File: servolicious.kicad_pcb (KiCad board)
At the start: 2 copper layers, 57.5 x 27.5 mm, 14 parts, among them J1 Conn_01x03_Pin, J10 Barrel_Jack_MountingPin, J2 Conn_01x03_Pin, J3 Conn_01x03_Pin, J4 Conn_01x03_Pin, J5 Conn_01x03_Pin, J6 Conn_01x03_Pin, J7 Conn_01x03_Pin, J8 Conn_01x03_Pin, J9 Conn_01x03_Pin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

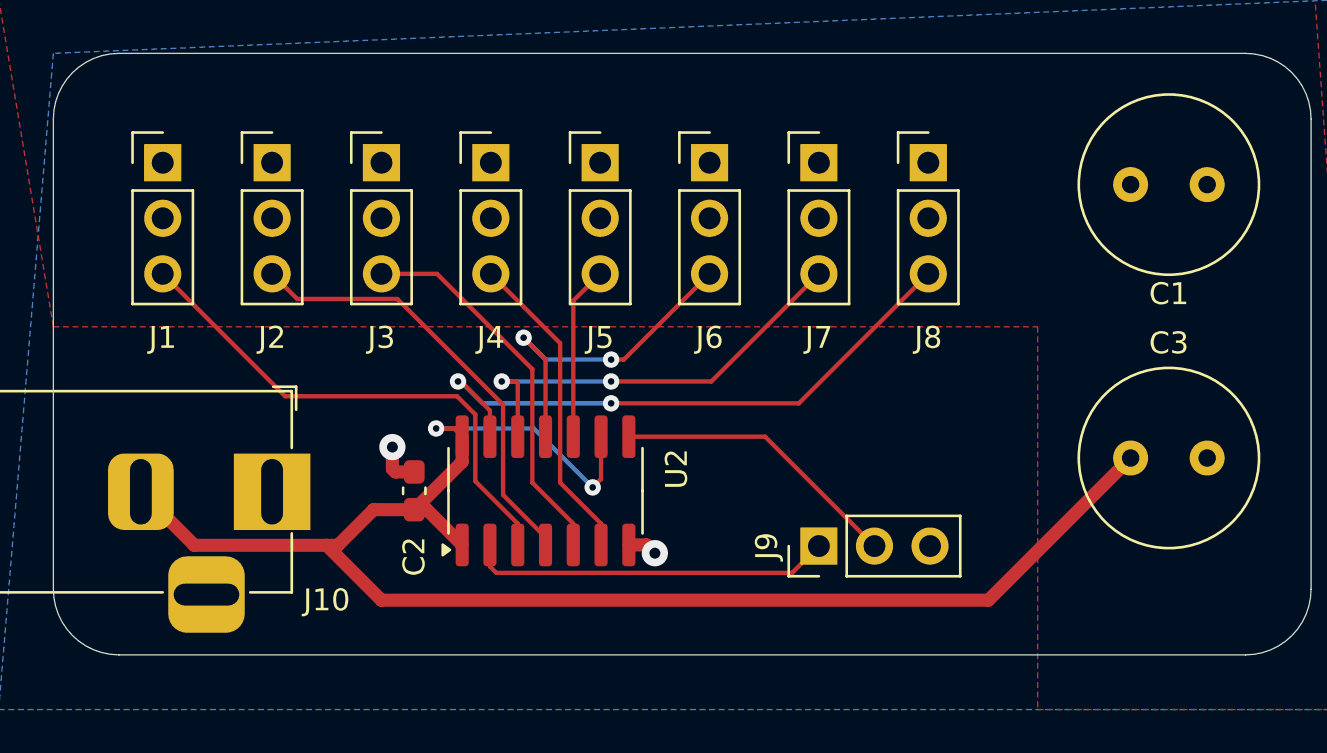
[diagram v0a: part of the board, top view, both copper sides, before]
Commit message: Switch to latched shift register
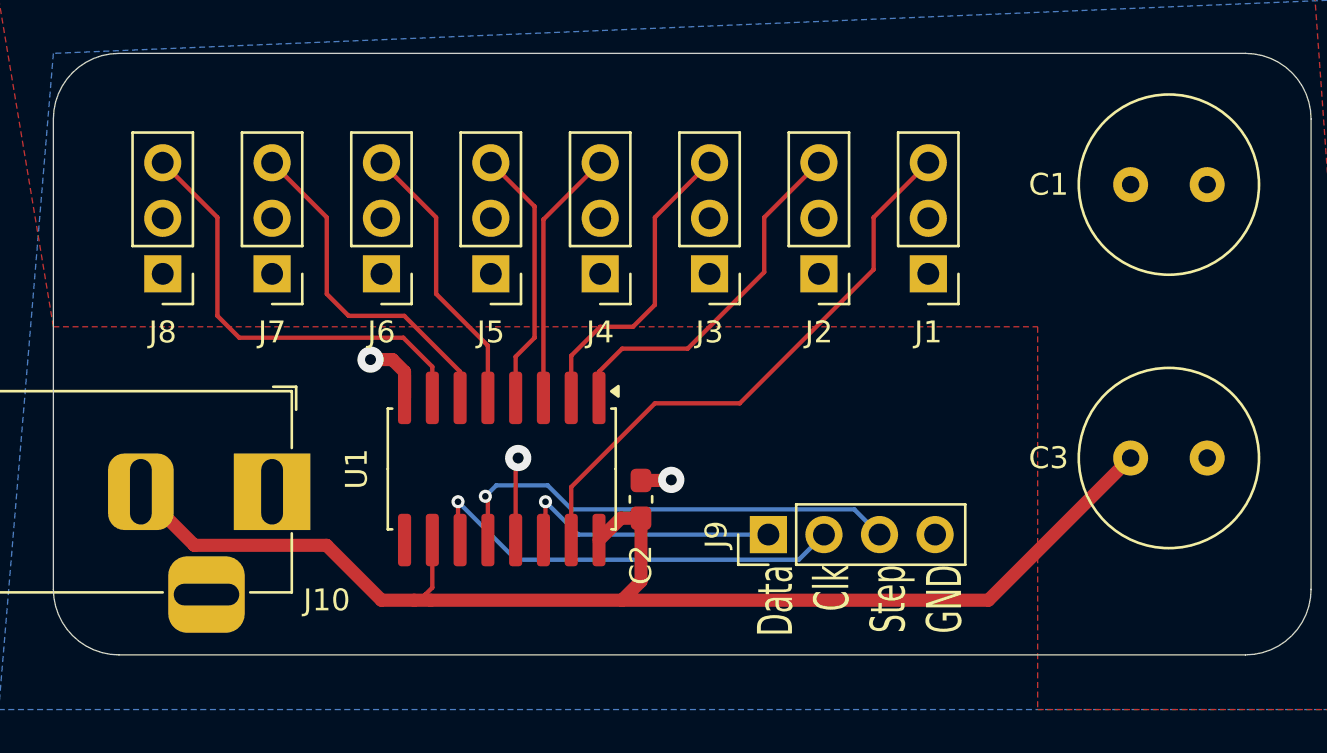
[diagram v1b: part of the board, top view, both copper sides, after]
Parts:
- removed U2: 74HC164, Package_SO:SOIC-14_3.9x8.7mm_P1.27mm
- added U1: 74AHC595, Package_SO:SOIC-16W_5.3x10.2mm_P1.27mm, F.Cu at (118.0, 114.0)
- J9: value Conn_01x03_Pin -> Conn_01x04_Pin; footprint Connector_PinHeader_2.54mm:PinHeader_1x03_P2.54mm_Vertical -> Connector_PinHeader_2.54mm:PinHeader_1x04_P2.54mm_Vertical
- moved J1 35.4 mm to (137.5, 105.1), turned to 180 degrees
- moved J8 35.4 mm to (102.5, 105.1), turned to 180 degrees
- moved J2 25.5 mm to (132.5, 105.1), turned to 180 degrees
- moved J7 25.5 mm to (107.5, 105.1), turned to 180 degrees
- moved J3 15.8 mm to (127.5, 105.1), turned to 180 degrees
- moved J6 15.8 mm to (112.5, 105.1), turned to 180 degrees
- moved C2 10.4 mm to (124.4, 115.4)
- moved J4 7.13 mm to (122.5, 105.1), turned to 180 degrees
- moved J5 7.13 mm to (117.5, 105.1), turned to 180 degrees
- moved J9 2.37 mm to (130.2, 117.0)
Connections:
- J9 pad 3: Earth -> /OUT
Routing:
- net /OUT: track 0.00 -> 21.2 mm, vias 0 -> 1
- net +5V: track 73.9 -> 59.7 mm, vias 2 -> 0
- net /Servo8: track 27.6 -> 20.2 mm, vias 2 -> 0
- net /CLK: track 13.3 -> 20.1 mm, vias 0 -> 1
- net Earth: track 3.40 -> 8.17 mm, vias 2 -> 3
- net /INP: track 16.7 -> 12.6 mm, vias 0 -> 1
- net /Servo5: track 7.95 -> 11.9 mm
- net /Servo7: track 19.8 -> 15.8 mm, vias 2 -> 0
- net /Servo2: track 20.3 -> 16.7 mm
- net /Servo3: track 17.5 -> 14.2 mm
- net /Servo6: track 15.5 -> 12.8 mm, vias 2 -> 0
- net /Servo4: track 14.5 -> 11.8 mm
- net /Servo1: track 23.7 -> 26.3 mm
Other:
- board text added: "Data Clk Step GND"

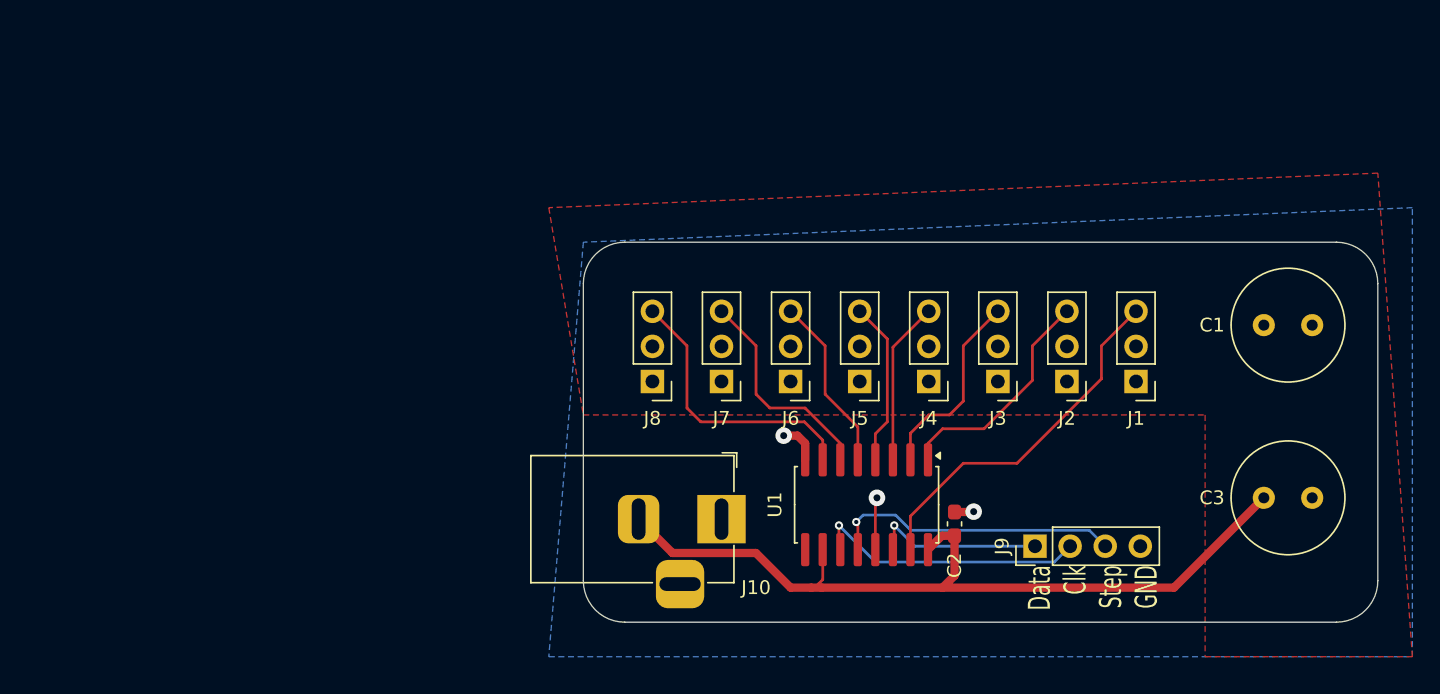
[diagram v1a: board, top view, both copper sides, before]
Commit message: Add daisy out
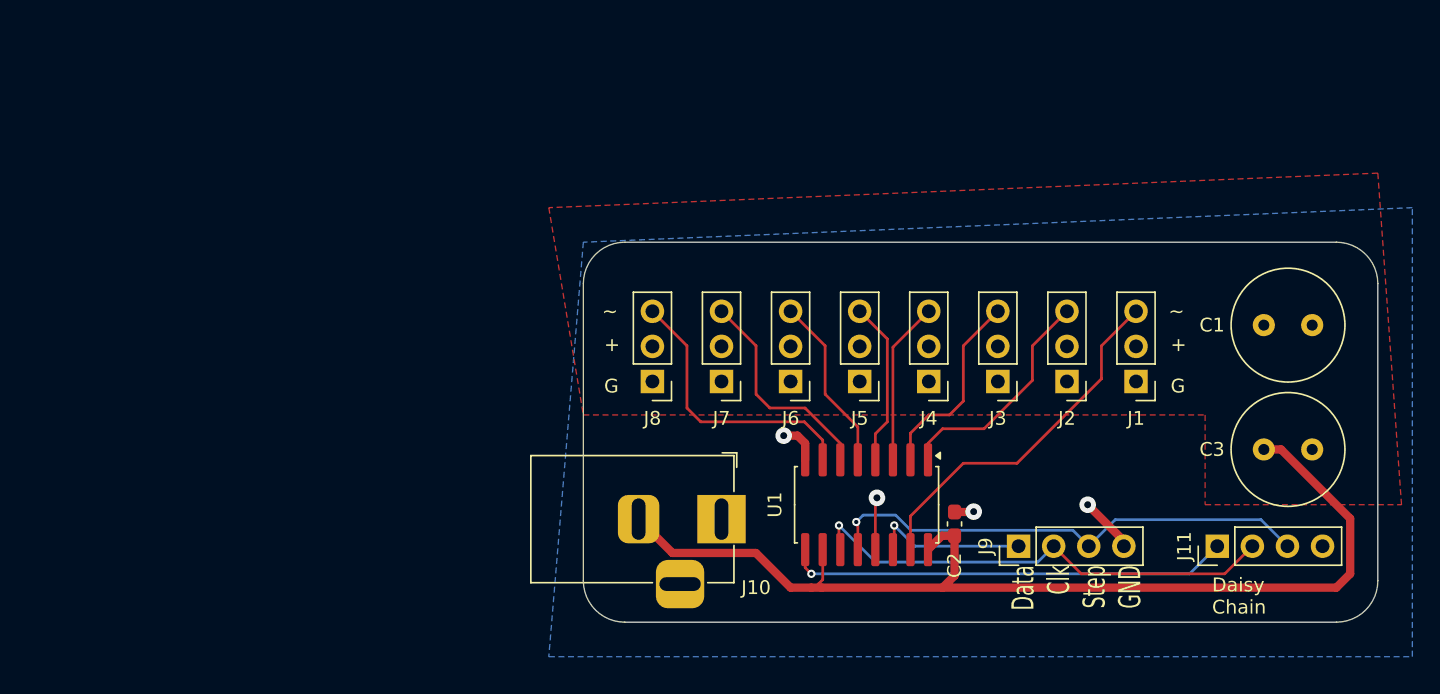
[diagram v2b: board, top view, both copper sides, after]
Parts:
- added J11: Conn_01x04_Pin, Connector_PinHeader_2.54mm:PinHeader_1x04_P2.54mm_Vertical, F.Cu at (143.4, 117.0)
- moved C3 3.50 mm to (146.8, 110.0)
- moved J9 1.19 mm to (129.0, 117.0)
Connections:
- U1 pad 9: unconnected-(U1-QH&apos;-Pad9) -> /CHAIN
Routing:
- net /CHAIN: track 0.00 -> 32.1 mm, vias 0 -> 1
- net +5V: track 59.7 -> 76.0 mm
- net /CLK: track 20.1 -> 34.9 mm
- net /OUT: track 21.2 -> 36.0 mm
- net Earth: track 8.17 -> 12.3 mm, vias 3 -> 4
- net /INP: track 12.6 -> 11.4 mm
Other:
- board text added: "+"
- board text added: "Daisy Chain"
- board text added: "G"
- board text added: "~"

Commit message: Use the PCA9685
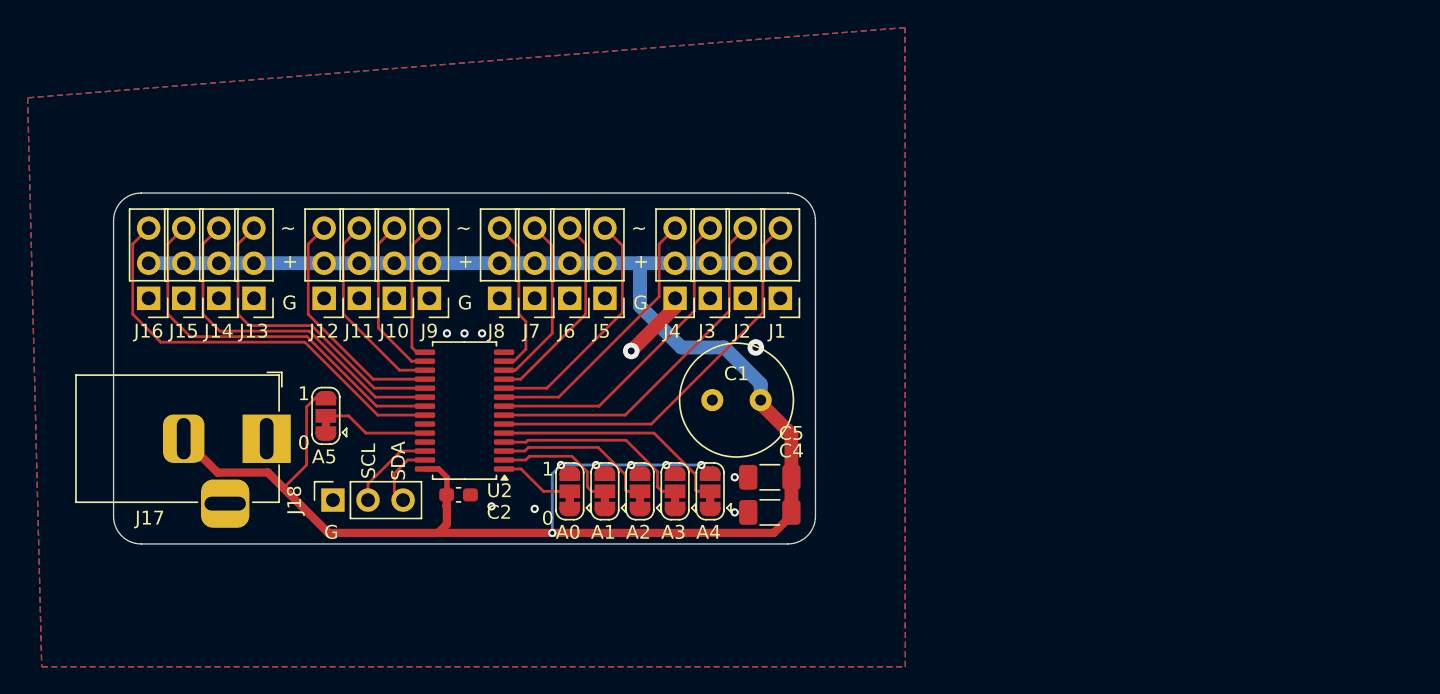
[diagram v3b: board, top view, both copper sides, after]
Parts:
- removed C3: C_Small_US, Capacitor_THT:C_Radial_D8.0mm_H11.5mm_P3.50mm
- removed U1: 74AHC595, Package_SO:SOIC-16W_5.3x10.2mm_P1.27mm
- added C4: C_Small, Capacitor_SMD:C_1206_3216Metric_Pad1.33x1.80mm_HandSolder, F.Cu at (111.0, 114.6)
- added C5: C_Small, Capacitor_SMD:C_1206_3216Metric_Pad1.33x1.80mm_HandSolder, F.Cu at (111.0, 112.0)
- added J12: Conn_01x03_Pin, Connector_PinHeader_2.54mm:PinHeader_1x03_P2.54mm_Vertical, F.Cu at (78.7, 99.1)
- added J13: Conn_01x03_Pin, Connector_PinHeader_2.54mm:PinHeader_1x03_P2.54mm_Vertical, F.Cu at (73.7, 99.1)
- added J14: Conn_01x03_Pin, Connector_PinHeader_2.54mm:PinHeader_1x03_P2.54mm_Vertical, F.Cu at (71.1, 99.1)
- added J15: Conn_01x03_Pin, Connector_PinHeader_2.54mm:PinHeader_1x03_P2.54mm_Vertical, F.Cu at (68.6, 99.1)
- added J16: Conn_01x03_Pin, Connector_PinHeader_2.54mm:PinHeader_1x03_P2.54mm_Vertical, F.Cu at (66.0, 99.1)
- added J17: Barrel_Jack_MountingPin, Connector_BarrelJack:BarrelJack_Horizontal, F.Cu at (74.6, 109.2)
- added J18: Conn_01x03, Connector_PinSocket_2.54mm:PinSocket_1x03_P2.54mm_Vertical, F.Cu at (79.4, 113.7)
- added JP1: Jumper:SolderJumper-3_P1.3mm_Bridged12_RoundedPad1.0x1.5mm, Jumper:SolderJumper-3_P1.3mm_Bridged12_RoundedPad1.0x1.5mm, F.Cu at (96.5, 113.0)
- added JP2: Jumper:SolderJumper-3_P1.3mm_Bridged12_RoundedPad1.0x1.5mm, Jumper:SolderJumper-3_P1.3mm_Bridged12_RoundedPad1.0x1.5mm, F.Cu at (99.1, 113.0)
- added JP3: Jumper:SolderJumper-3_P1.3mm_Bridged12_RoundedPad1.0x1.5mm, Jumper:SolderJumper-3_P1.3mm_Bridged12_RoundedPad1.0x1.5mm, F.Cu at (101.6, 113.0)
- added JP4: Jumper:SolderJumper-3_P1.3mm_Bridged12_RoundedPad1.0x1.5mm, Jumper:SolderJumper-3_P1.3mm_Bridged12_RoundedPad1.0x1.5mm, F.Cu at (104.1, 113.0)
- added JP5: Jumper:SolderJumper-3_P1.3mm_Bridged12_RoundedPad1.0x1.5mm, Jumper:SolderJumper-3_P1.3mm_Bridged12_RoundedPad1.0x1.5mm, F.Cu at (106.7, 113.0)
- added JP6: Jumper:SolderJumper-3_P1.3mm_Bridged12_RoundedPad1.0x1.5mm, Jumper:SolderJumper-3_P1.3mm_Bridged12_RoundedPad1.0x1.5mm, F.Cu at (78.9, 107.6)
- added U2: PCA9685PW, Package_SO:TSSOP-28_4.4x9.7mm_P0.65mm, F.Cu at (88.9, 107.2)
- J10: value Barrel_Jack_MountingPin -> Conn_01x03_Pin; footprint Connector_BarrelJack:BarrelJack_Horizontal -> Connector_PinHeader_2.54mm:PinHeader_1x03_P2.54mm_Vertical
- J11, J9: value Conn_01x04_Pin -> Conn_01x03_Pin; footprint Connector_PinHeader_2.54mm:PinHeader_1x04_P2.54mm_Vertical -> Connector_PinHeader_2.54mm:PinHeader_1x03_P2.54mm_Vertical
- moved J11 64.6 mm to (81.3, 99.1), turned to 180 degrees
- moved J9 46.3 mm to (86.4, 99.1), turned to 180 degrees
- moved C1 36.8 mm to (110.3, 106.4), turned to 180 degrees
- moved C2 36.0 mm to (88.5, 113.3), turned to 0 degrees
- moved J10 28.6 mm to (83.8, 99.1), turned to 180 degrees
- moved J1 26.4 mm to (111.8, 99.1)
- moved J2 24.0 mm to (109.2, 99.1)
- moved J3 21.7 mm to (106.7, 99.1)
- moved J5 19.4 mm to (99.1, 99.1)
- moved J4 19.3 mm to (104.1, 99.1)
- moved J6 17.1 mm to (96.5, 99.1)
- moved J7 14.8 mm to (94.0, 99.1)
- moved J8 12.6 mm to (91.4, 99.1)
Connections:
- J10 pad 3: (no net) -> /Servo10
- J11 pad 1: /CHAIN -> Earth
- J11 pad 2: /CLK -> +5V
- J11 pad 3: /OUT -> /Servo11
- J9 pad 1: /INP -> Earth
- J9 pad 2: /CLK -> +5V
- J9 pad 3: /OUT -> /Servo9
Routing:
- net +5V: track 76.0 -> 151.8 mm, vias 0 -> 6
- net /OUT: track 36.0 -> 0.00 mm, vias 1 -> 0
- net /CLK: track 34.9 -> 0.00 mm, vias 1 -> 0
- net /CHAIN: track 32.1 -> 0.00 mm, vias 1 -> 0
- net /Servo16: track 0.00 -> 30.9 mm
- net /Servo15: track 0.00 -> 28.1 mm
- net /Servo14: track 0.00 -> 25.3 mm
- net /Servo13: track 0.00 -> 22.5 mm
- net /A4: track 0.00 -> 17.3 mm
- net /Servo12: track 0.00 -> 17.1 mm
- net /A3: track 0.00 -> 14.6 mm
- net /Servo11: track 0.00 -> 14.3 mm
- net /Servo10: track 0.00 -> 12.1 mm
- net /A2: track 0.00 -> 11.9 mm
- net /INP: track 11.4 -> 0.00 mm, vias 1 -> 0
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- added copper zone on F.Cu, net Earth
- removed copper zone on F.Cu, net +5V
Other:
- board size 57.5 x 27.5 mm -> 50.8 x 25.4 mm
- board text added: "0"
- board text added: "1"
- board text added: "A0"
- board text added: "A1"
- board text added: "A2"
- board text added: "A3"
- board text added: "A4"
- board text added: "A5"
- board text added: "SCL"
- board text added: "SDA"
- board text removed: "Daisy Chain"
- board text removed: "Data Clk Step GND"
